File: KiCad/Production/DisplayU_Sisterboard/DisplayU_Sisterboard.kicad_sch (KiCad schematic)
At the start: 0 parts

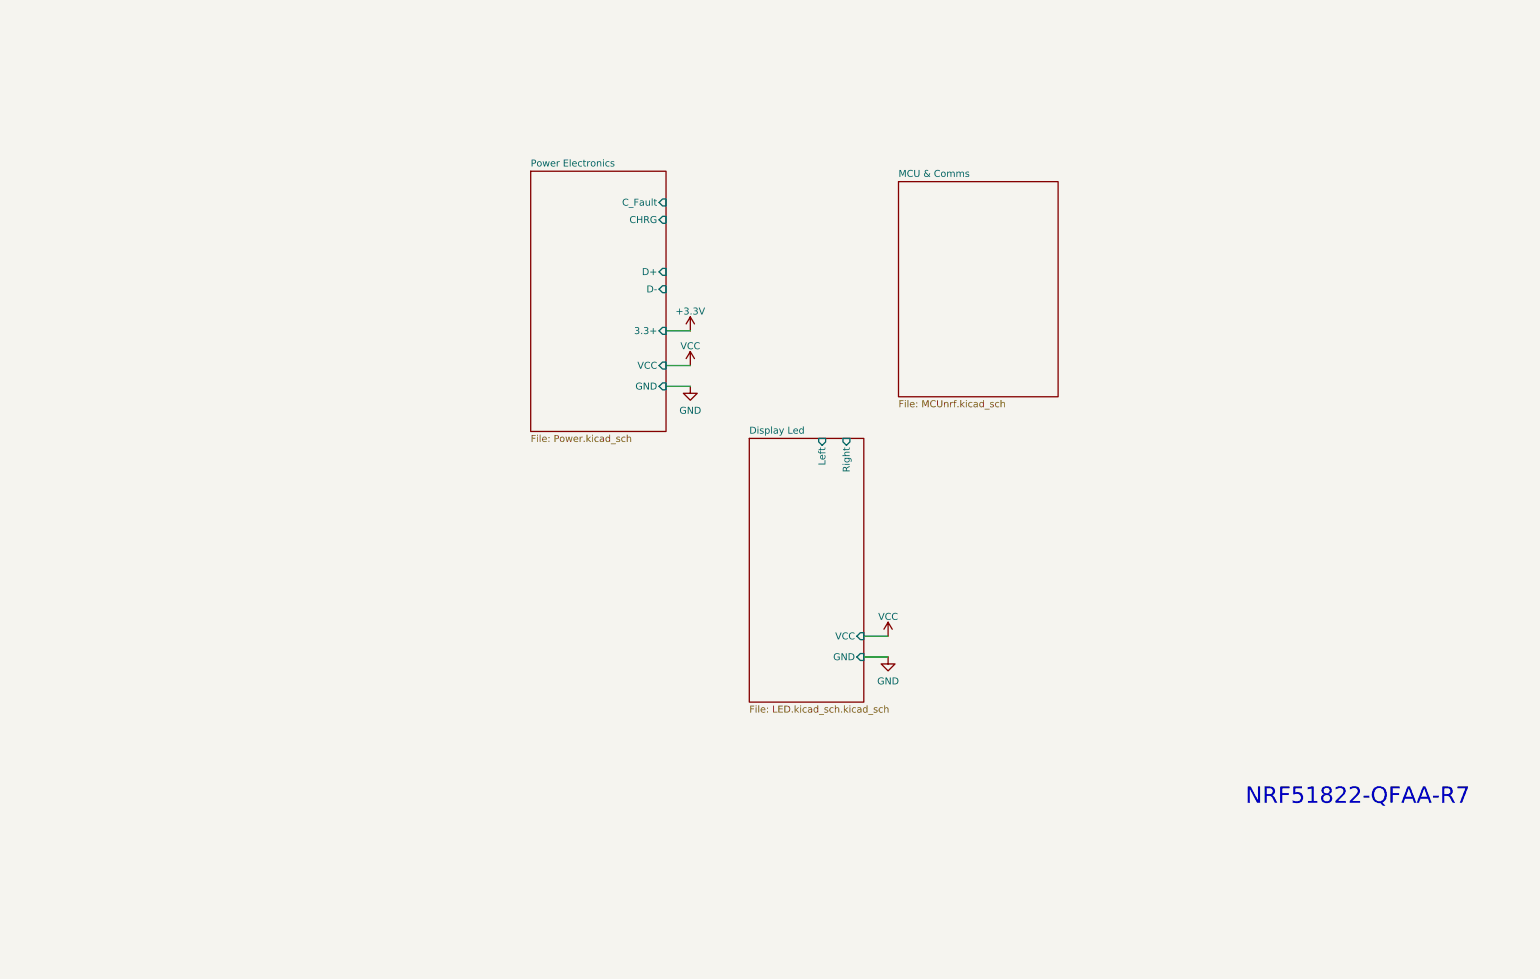
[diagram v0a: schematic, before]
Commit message: Display U is like 99% finished
- BMS Chips prob not needed
- LDO Chip prob not needed
- Final touches
> Start on routing
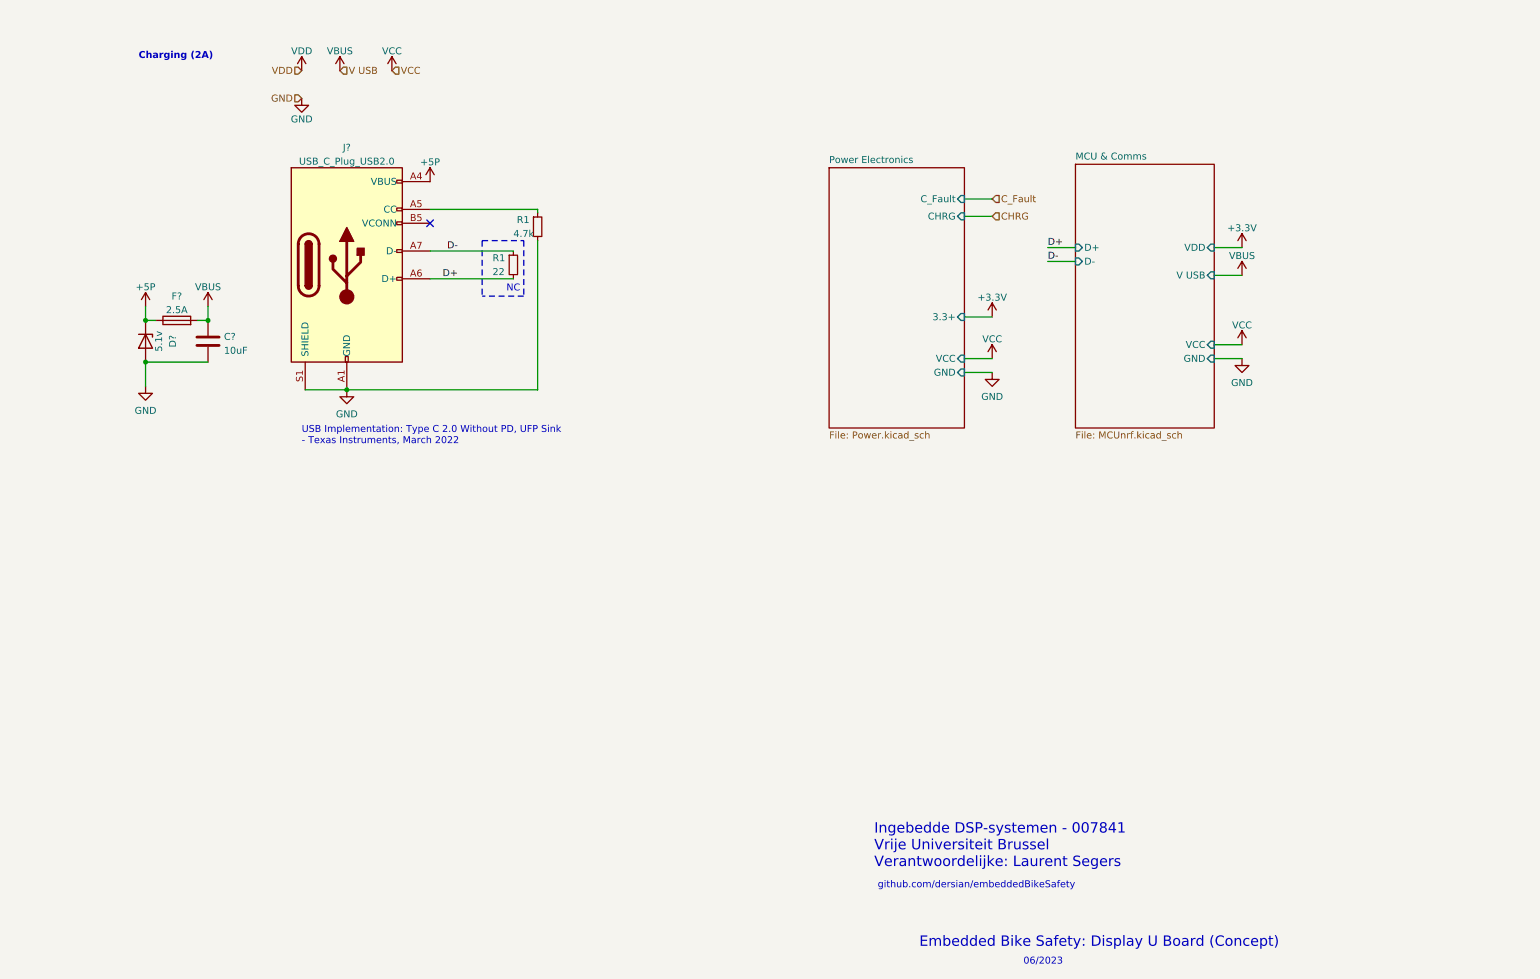
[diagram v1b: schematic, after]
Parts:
- added C?: 10uF, Capacitor_SMD:C_0603_1608Metric_Pad1.08x0.95mm_HandSolder, symbol Device:C
- added D?: 5.1v, symbol Device:D_Zener
- added F?: 2.5A, symbol Device:Fuse
- added J?: USB_C_Plug_USB2.0, Connector_USB:USB_C_Receptacle_GCT_USB4135-GF-A_6P_TopMnt_Horizontal, symbol Connector:USB_C_Plug_USB2.0
- added R1: 22, symbol Device:R_Small
- added R1: 4.7k, symbol Device:R_Small
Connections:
- net GND: now also C?.2, D?.2 (A), J?.A1 (GND), J?.A12 (GND), J?.B1 (GND), J?.B12 (GND), J?.S1 (SHIELD), R1.2
- new net: J?.A5 (CC), R1.1
- new net +5P: D?.1 (K), F?.1, J?.A4 (VBUS), J?.A9 (VBUS), J?.B4 (VBUS), J?.B9 (VBUS)
- new net D+: J?.A6 (D+), R1.2
- new net D-: J?.A7 (D-), R1.1
- new net VBUS: C?.1, F?.2
- no-connect marks 0 -> 1
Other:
- removed sheet Display Led
- sheet MCU & Comms ports: added D+, D-, GND, V USB, VCC, VDD; removed none
- sheet Power Electronics ports: added none; removed D+, D-
- note added: "06/2023"
- note added: "Charging (2A)"
- note added: "Embedded Bike Safety: Display U Board (Concept)"
- note added: "Ingebedde DSP-systemen - 007841 Vrije Universiteit Brussel Verantwoordelijke: Laurent Segers"
- note added: "NC"
- note added: "USB Implementation: Type C 2.0 Without PD, UFP Sink - Texas Instruments, March 2022"
- note added: "github.com/dersian/embeddedBikeSafety"
- note removed: "NRF51822-QFAA-R7"

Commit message: Schematic is done
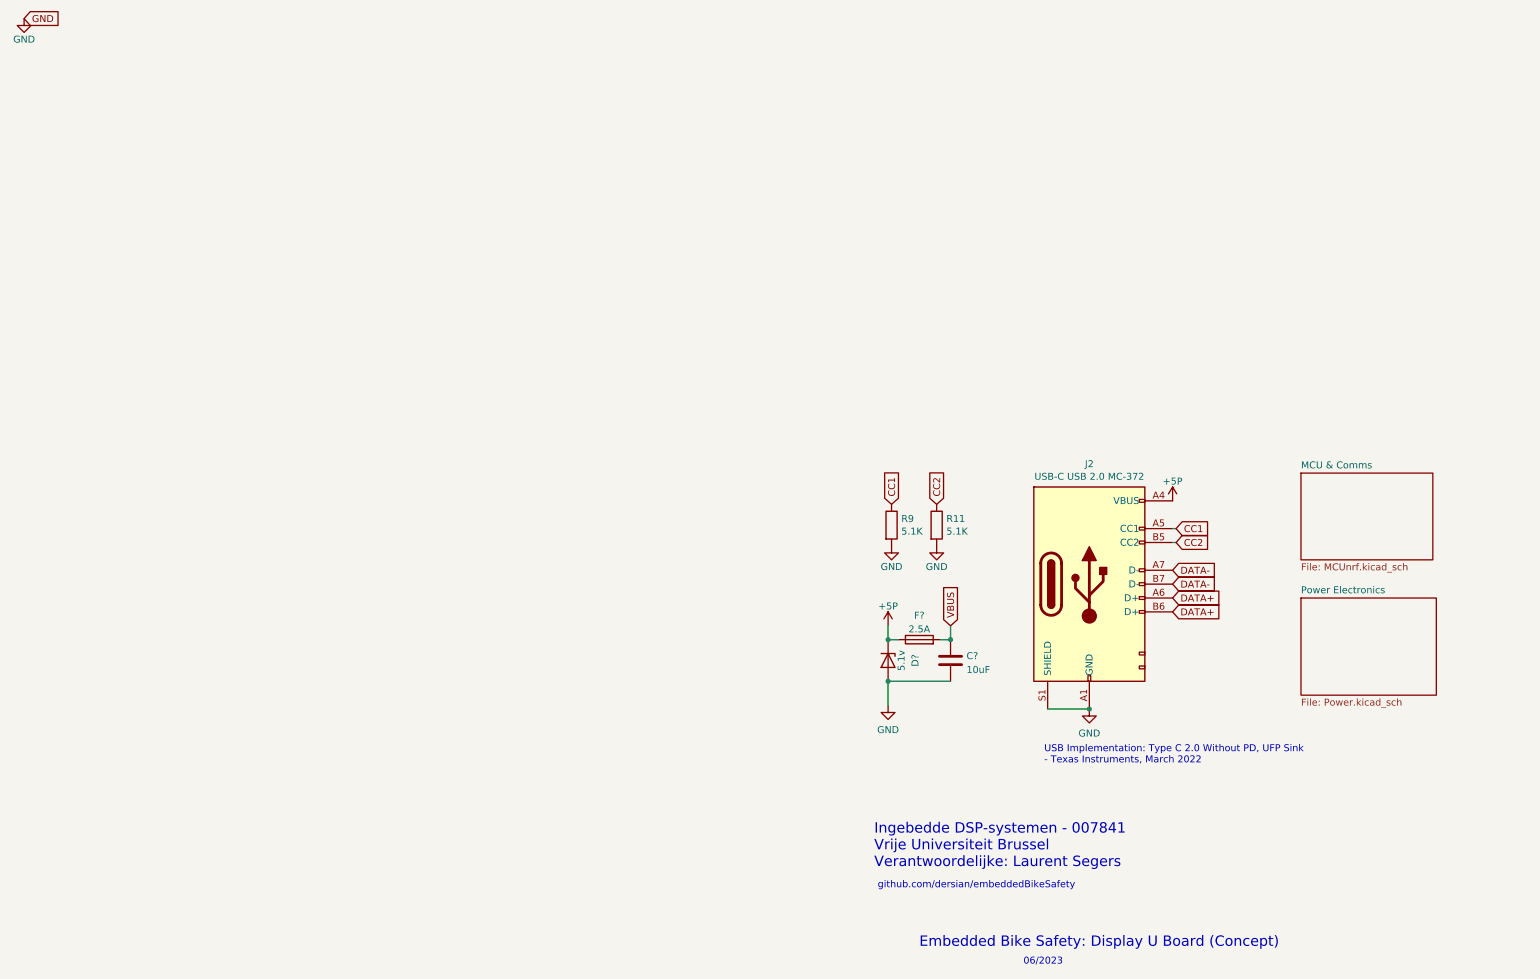
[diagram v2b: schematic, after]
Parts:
- removed J?: USB_C_Plug_USB2.0, Connector_USB:USB_C_Receptacle_GCT_USB4135-GF-A_6P_TopMnt_Horizontal, symbol Connector:USB_C_Plug_USB2.0
- removed R1: 22, symbol Device:R_Small
- removed R1: 4.7k, symbol Device:R_Small
- added J2: USB-C USB 2.0 MC-372, USB-C, symbol nrfmicro:USB_C_Receptacle_USB2.0
- added R11, R9: 5.1K, Resistor_SMD:R_0603_1608Metric, symbol Device:R
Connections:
- net +5P: now also J2.A4 (VBUS)
- net GND: now also J2.A1 (GND), J2.S1 (SHIELD), R11.2, R9.2
- new net CC1: J2.A5 (CC1), R9.1
- new net CC2: J2.B5 (CC2), R11.1
- new net DATA+: J2.A6 (D+), J2.B6 (D+)
- new net DATA-: J2.A7 (D-), J2.B7 (D-)
- no-connect marks 1 -> 0
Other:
- sheet MCU & Comms ports: added none; removed D+, D-, GND, V USB, VCC, VDD
- sheet Power Electronics ports: added none; removed 3.3+, CHRG, C_Fault, GND, VCC
- note removed: "Charging (2A)"
- note removed: "NC"
- moved on the sheet: C?, D?, F?

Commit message: Routing
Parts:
- removed F?: 2.5A, symbol Device:Fuse
- D?: value 5.1v -> BZT52C5V6S-7-F; footprint (none) -> Diode_SMD:D_SOD-323F
- J2: footprint USB-C -> VUBRacing_ELO:USB C 2.0 MC 772
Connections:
- net +5P is gone; now on net VBUS: D?.1 (K), J2.A4 (VBUS)
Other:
- note added: "- Sam Dilmaghanian"
- moved on the sheet: C?, D?, R11, R9

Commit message: Berekening/Metingen Verslag
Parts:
- J2: value USB-C USB 2.0 MC-372 -> USB4105-GF-A
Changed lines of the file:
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@@
       (effects (font (size 1.27 1.27)))
     )
-    (property "Value" "USB-C USB 2.0 MC-372" (at 217.17 104.775 0)
+    (property "Value" "USB4105-GF-A\n" (at 217.17 104.775 0)
       (effects (font (size 1.27 1.27)))
     )
